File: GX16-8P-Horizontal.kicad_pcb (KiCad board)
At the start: 2 copper layers, 24.1 x 15.9 mm, 2 parts, among them J1 GX16, J2 Board Header

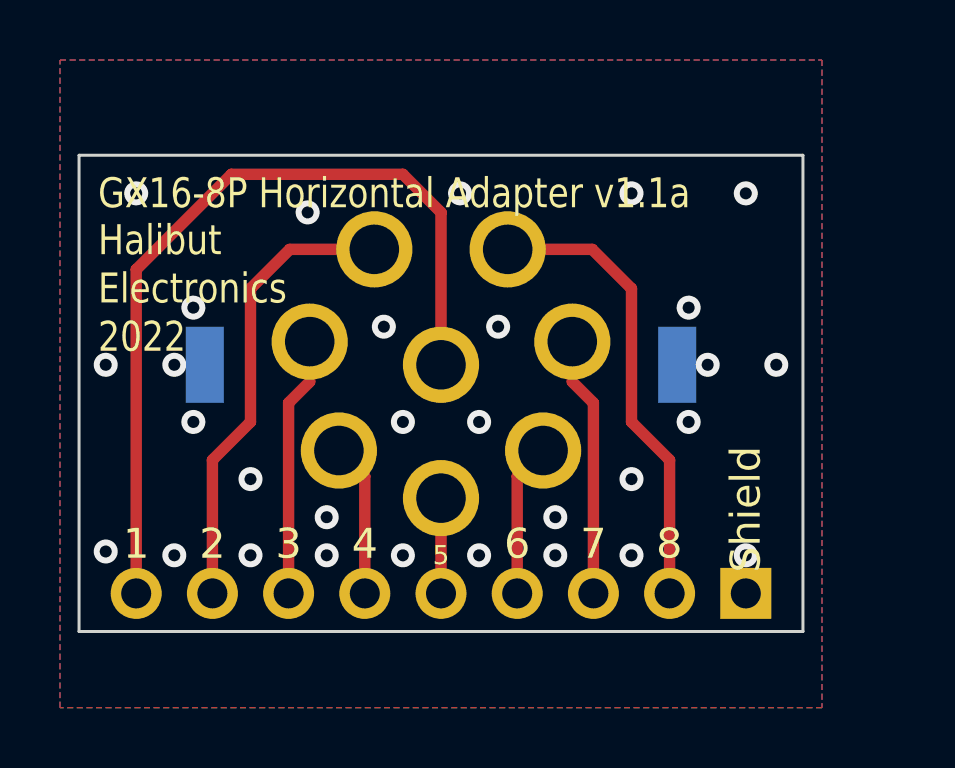
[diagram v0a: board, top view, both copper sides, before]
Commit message: Updated the GX16 based on the drawing from the manufacturer. Brought pins in a bit. Wrote a python script to do the math to give me exact locations.
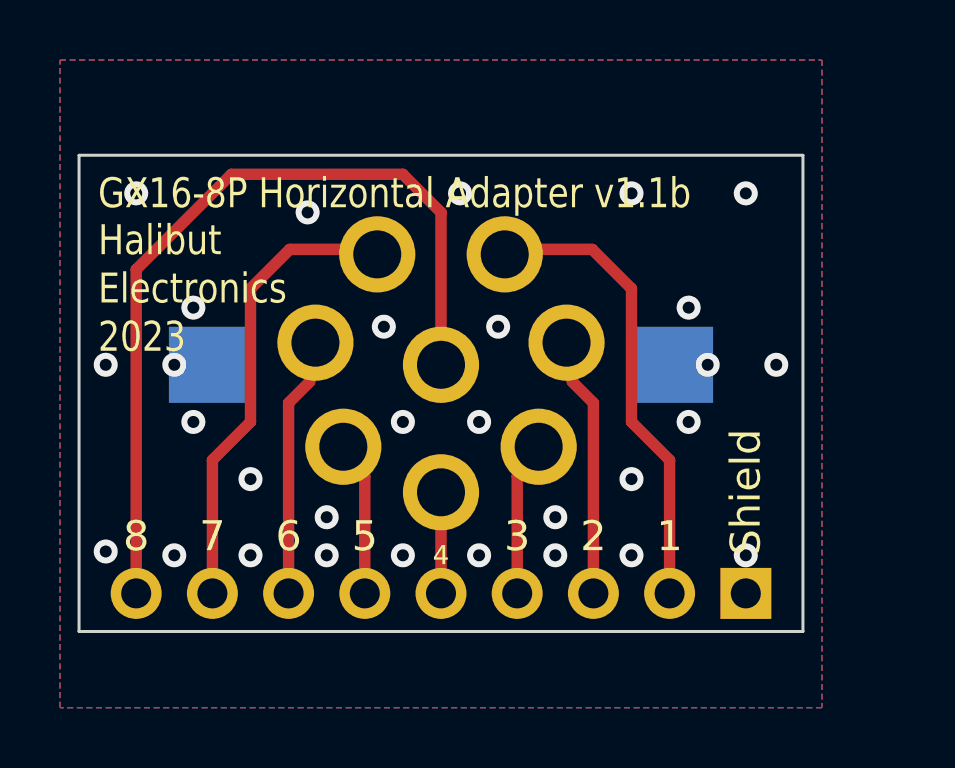
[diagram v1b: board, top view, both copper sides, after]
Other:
- board text added: "GX16-8P Horizontal Adapter v1.1b"
- board text added: "Halibut Electronics 2023"
- board text removed: "GX16-8P Horizontal Adapter v1.1a"
- board text removed: "Halibut Electronics 2022"
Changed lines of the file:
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@@
       (effects (font (size 1 1) (thickness 0.15)) (justify mirror))
     )
+    (fp_line (start 9.398 -5.42544) (end 9.398 5.42544) (layer "B.SilkS") (width 0.12))
+    (fp_line (start 0 10.8458) (end 9.398 5.42544) (layer "B.SilkS") (width 0.12))
     (fp_line (start 0 10.8458) (end -9.398 5.42544) (layer "B.SilkS") (width 0.12))
+    (fp_line (start 0 7.366) (end -2.794 7.366) (layer "B.SilkS") (width 0.12))
+    (fp_line (start 0 -10.8458) (end 9.398 -5.42544) (layer "B.SilkS") (width 0.12))
     (fp_line (start -9.398 -5.42544) (end -9.398 5.42544) (layer "B.SilkS") (width 0.12))
-    (fp_line (start 0 10.8458) (end 9.398 5.42544) (layer "B.SilkS") (width 0.12))
-    (fp_line (start 9.398 -5.42544) (end 9.398 5.42544) (layer "B.SilkS") (width 0.12))
-    (fp_line (start 7.366 0) (end 7.366 2.794) (layer "B.SilkS") (width 0.12))
-    (fp_line (start 7.366 0) (end 7.366 -2.794) (layer "B.SilkS") (width 0.12))
-    (fp_line (start 0 -10.8458) (end 9.398 -5.42544) (layer "B.SilkS") (width 0.12))
-    (fp_line (start -7.366 0) (end -7.366 -2.794) (layer "B.SilkS") (width 0.12))
-    (fp_line (start -7.366 0) (end -7.366 2.794) (layer "B.SilkS") (width 0.12))
     (fp_line (start -9.398 -5.42544) (end 0 -10.8458) (layer "B.SilkS") (width 0.12))
-    (fp_arc (start 7.365999 2.794) (mid 0 7.878095) (end -7.365999 2.794) (layer "B.SilkS") (width 0.12))
-    (fp_arc (start -7.365999 -2.794) (mid 0 -7.878095) (end 7.365999 -2.794) (layer "B.SilkS") (width 0.12))
+    (fp_line (start 0 7.366) (end 2.794 7.366) (layer "B.SilkS") (width 0.12))
+    (fp_arc (start -2.794 7.365999) (mid -7.878095 0) (end -2.794 -7.365999) (layer "B.SilkS") (width 0.12))
+    (fp_arc (start 2.794 -7.365999) (mid 7.878095 0) (end 2.794 7.365999) (layer "B.SilkS") (width 0.12))
+    (fp_arc (start -2.794 -7.365998) (mid 0 -7.878094) (end 2.794 -7.365998) (layer "B.SilkS") (width 0.12))
     (fp_circle (center 0 0) (end 9.144 0) (layer "B.SilkS") (width 0.12) (fill none))
     (fp_circle (center 0 0) (end 8.382 0) (layer "B.CrtYd") (width 0.05) (fill none))
-    (pad "1" thru_hole circle (at -2.2225 3.8481 180) (size 2.54 2.54) (drill 1.651) (layers *.Cu *.Mask)
+    (pad "1" thru_hole circle (at -2.125 3.681 180) (size 2.54 2.54) (drill 1.6) (layers *.Cu *.Mask)
       (net 1 "Net-(J1-Pad1)") (pinfunction "Pin_1") (pintype "passive"))
-    (pad "2" thru_hole circle (at -4.37642 0.77216 180) (size 2.54 2.54) (drill 1.651) (layers *.Cu *.Mask)
+    (pad "2" thru_hole circle (at -4.185 0.738 180) (size 2.54 2.54) (drill 1.6) (layers *.Cu *.Mask)
       (net 2 "Net-(J1-Pad2)") (pinfunction "Pin_2") (pintype "passive"))
-    (pad "3" thru_hole circle (at -3.4036 -2.8575 180) (size 2.54 2.54) (drill 1.651) (layers *.Cu *.Mask)
+    (pad "3" thru_hole circle (at -3.256 -2.732 180) (size 2.54 2.54) (drill 1.6) (layers *.Cu *.Mask)
       (net 3 "Net-(J1-Pad3)") (pinfunction "Pin_3") (pintype "passive"))
-    (pad "4" thru_hole circle (at 0 -4.445 180) (size 2.54 2.54) (drill 1.651) (layers *.Cu *.Mask)
+    (pad "4" thru_hole circle (at 0 -4.25 180) (size 2.54 2.54) (drill 1.6) (layers *.Cu *.Mask)
       (net 4 "Net-(J1-Pad4)") (pinfunction "Pin_4") (pintype "passive"))
-    (pad "5" thru_hole circle (at 3.4036 -2.8575 180) (size 2.54 2.54) (drill 1.651) (layers *.Cu *.Mask)
+    (pad "5" thru_hole circle (at 3.256 -2.732 180) (size 2.54 2.54) (drill 1.6) (layers *.Cu *.Mask)
       (net 5 "Net-(J1-Pad5)") (pinfunction "Pin_5") (pintype "passive"))
-    (pad "6" thru_hole circle (at 4.37642 0.77216 180) (size 2.54 2.54) (drill 1.651) (layers *.Cu *.Mask)
+    (pad "6" thru_hole circle (at 4.185 0.738 180) (size 2.54 2.54) (drill 1.6) (layers *.Cu *.Mask)
       (net 6 "Net-(J1-Pad6)") (pinfunction "Pin_6") (pintype "passive"))
-    (pad "7" thru_hole circle (at 2.2225 3.8481 180) (size 2.54 2.54) (drill 1.651) (layers *.Cu *.Mask)
+    (pad "7" thru_hole circle (at 2.125 3.681 180) (size 2.54 2.54) (drill 1.6) (layers *.Cu *.Mask)
       (net 7 "Net-(J1-Pad7)") (pinfunction "Pin_7") (pintype "passive"))
-    (pad "8" thru_hole circle (at 0 0 180) (size 2.54 2.54) (drill 1.651) (layers *.Cu *.Mask)
+    (pad "8" thru_hole circle (at 0 0 180) (size 2.54 2.54) (drill 1.6) (layers *.Cu *.Mask)
       (net 8 "Net-(J1-Pad8)") (pinfunction "Pin_8") (pintype "passive"))
-    (pad "MP" smd rect (at -7.874 0 180) (size 1.27 2.54) (layers "B.Cu" "B.Paste" "B.Mask")
+    (pad "MP" smd rect (at -7.8 0 180) (size 2.54 2.54) (layers "B.Cu" "B.Paste" "B.Mask")
       (net 9 "GND") (pinfunction "MountPin") (pintype "passive"))
-    (pad "MP" smd rect (at 7.874 0 180) (size 1.27 2.54) (layers "B.Cu" "B.Paste" "B.Mask")
+    (pad "MP" smd rect (at 7.8 0 180) (size 2.54 2.54) (layers "B.Cu" "B.Paste" "B.Mask")
       (net 9 "GND") (pinfunction "MountPin") (pintype "passive"))
   )
@@
   )
   (gr_rect (start 139.065 72.39) (end 114.935 56.515) (layer "Edge.Cuts") (width 0.1) (fill none))
-  (gr_text "Shield" (at 137.16 70.425 90) (layer "F.SilkS")
+  (gr_text "Shield" (at 137.16 69.85 90) (layer "F.SilkS")
     (effects (font (size 1 1) (thickness 0.15)) (justify left))
   )
-  (gr_text "7" (at 132.08 69.469) (layer "F.SilkS")
+  (gr_text "7" (at 119.38 69.215) (layer "F.SilkS")
     (effects (font (size 1 1) (thickness 0.15)))
   )
-  (gr_text "1" (at 116.84 69.469) (layer "F.SilkS")
+  (gr_text "1" (at 134.62 69.215) (layer "F.SilkS")
     (effects (font (size 1 1) (thickness 0.15)))
   )
-  (gr_text "GX16-8P Horizontal Adapter v1.1a\n" (at 115.57 57.785) (layer "F.SilkS")
+  (gr_text "GX16-8P Horizontal Adapter v1.1b\n" (at 115.57 57.785) (layer "F.SilkS")
     (effects (font (size 1 0.8382) (thickness 0.15)) (justify left))
   )
-  (gr_text "Halibut\nElectronics\n2022" (at 115.57 60.96) (layer "F.SilkS")
+  (gr_text "Halibut\nElectronics\n2023" (at 115.57 60.96) (layer "F.SilkS")
     (effects (font (size 1 0.8382) (thickness 0.15)) (justify left))
   )
-  (gr_text "5" (at 127 69.85) (layer "F.SilkS")
+  (gr_text "4" (at 127 69.85) (layer "F.SilkS")
     (effects (font (size 0.635 0.635) (thickness 0.1016)))
   )
-  (gr_text "4" (at 124.46 69.469) (layer "F.SilkS")
+  (gr_text "5" (at 124.46 69.215) (layer "F.SilkS")
     (effects (font (size 1 1) (thickness 0.15)))
   )
-  (gr_text "8" (at 134.608875 69.464072) (layer "F.SilkS")
+  (gr_text "8" (at 116.84 69.215) (layer "F.SilkS")
     (effects (font (size 1 1) (thickness 0.15)))
   )
-  (gr_text "6" (at 129.54 69.469) (layer "F.SilkS")
+  (gr_text "6" (at 121.92 69.215) (layer "F.SilkS")
     (effects (font (size 1 1) (thickness 0.15)))
   )
-  (gr_text "3" (at 121.92 69.469) (layer "F.SilkS")
+  (gr_text "3" (at 129.54 69.215) (layer "F.SilkS")
     (effects (font (size 1 1) (thickness 0.15)))
   )
-  (gr_text "2" (at 119.38 69.469) (layer "F.SilkS")
+  (gr_text "2" (at 132.08 69.215) (layer "F.SilkS")
     (effects (font (size 1 1) (thickness 0.15)))
   )
